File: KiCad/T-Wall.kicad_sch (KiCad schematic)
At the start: 52 parts, among them J1 IDC, J2 IDC, J3 IDC, J4 IDC, J5 IDC, J6 IDC, J7 IDC, J8 IDC, J9 2086-1107/300-000/997-607, U1 TCA9555PWR, U2 TCA9555PWR, U3 TCA9555PWR, U4 TCA9555PWR, U5 ESP32-S3-DevKitC, U6 SN74AHCT125RGYR, U9 TPS62A01APDDC

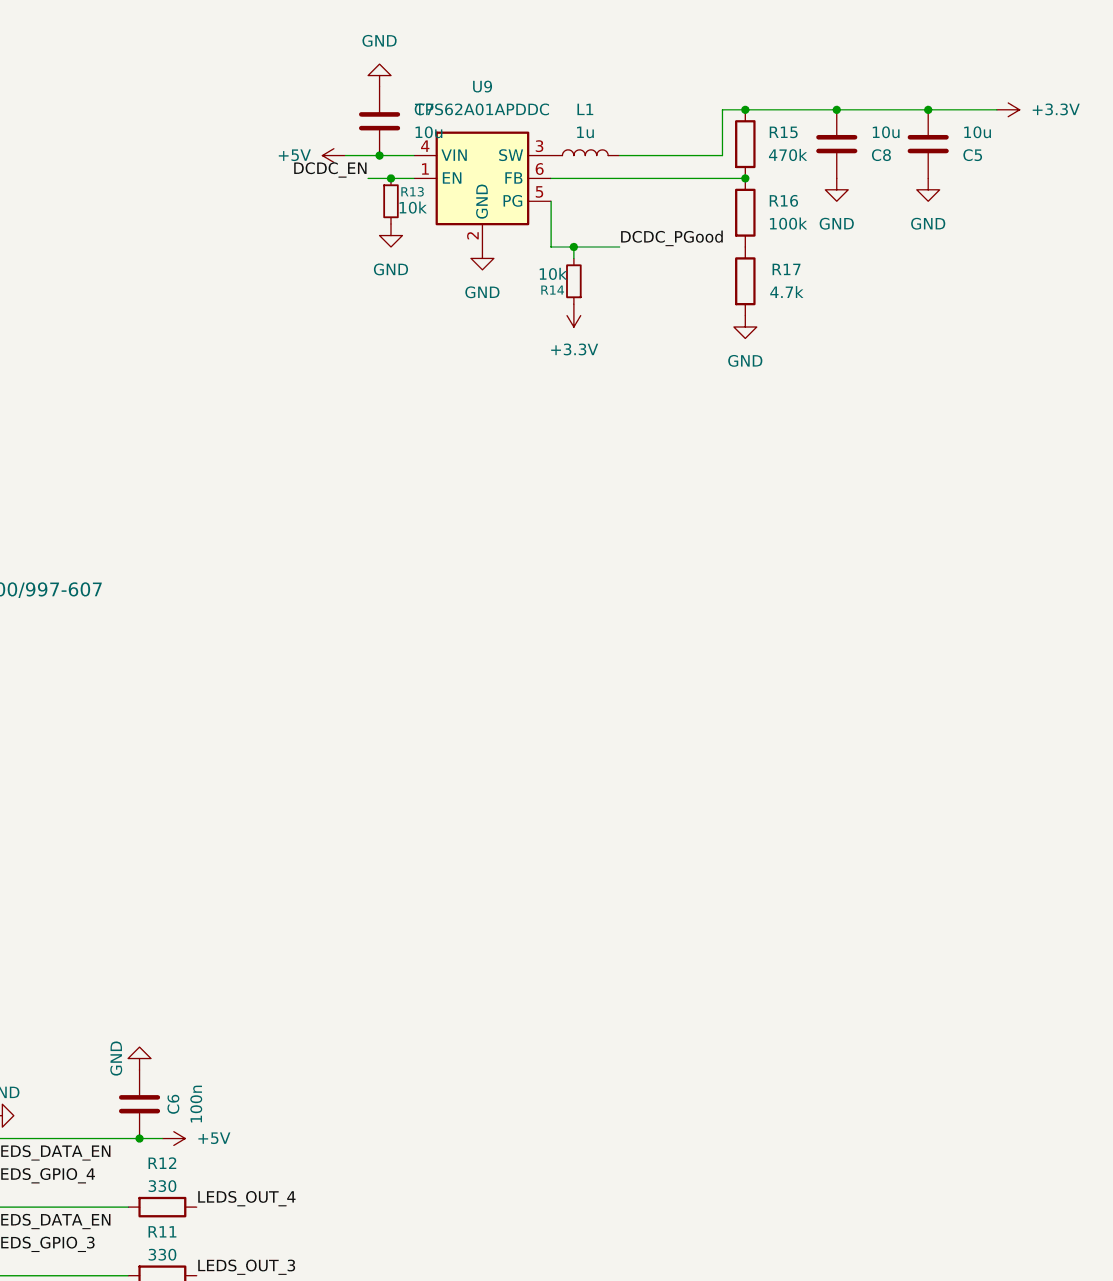
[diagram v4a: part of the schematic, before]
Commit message: PCB QOL: changed sizes to 0603 and moved vias away from pads
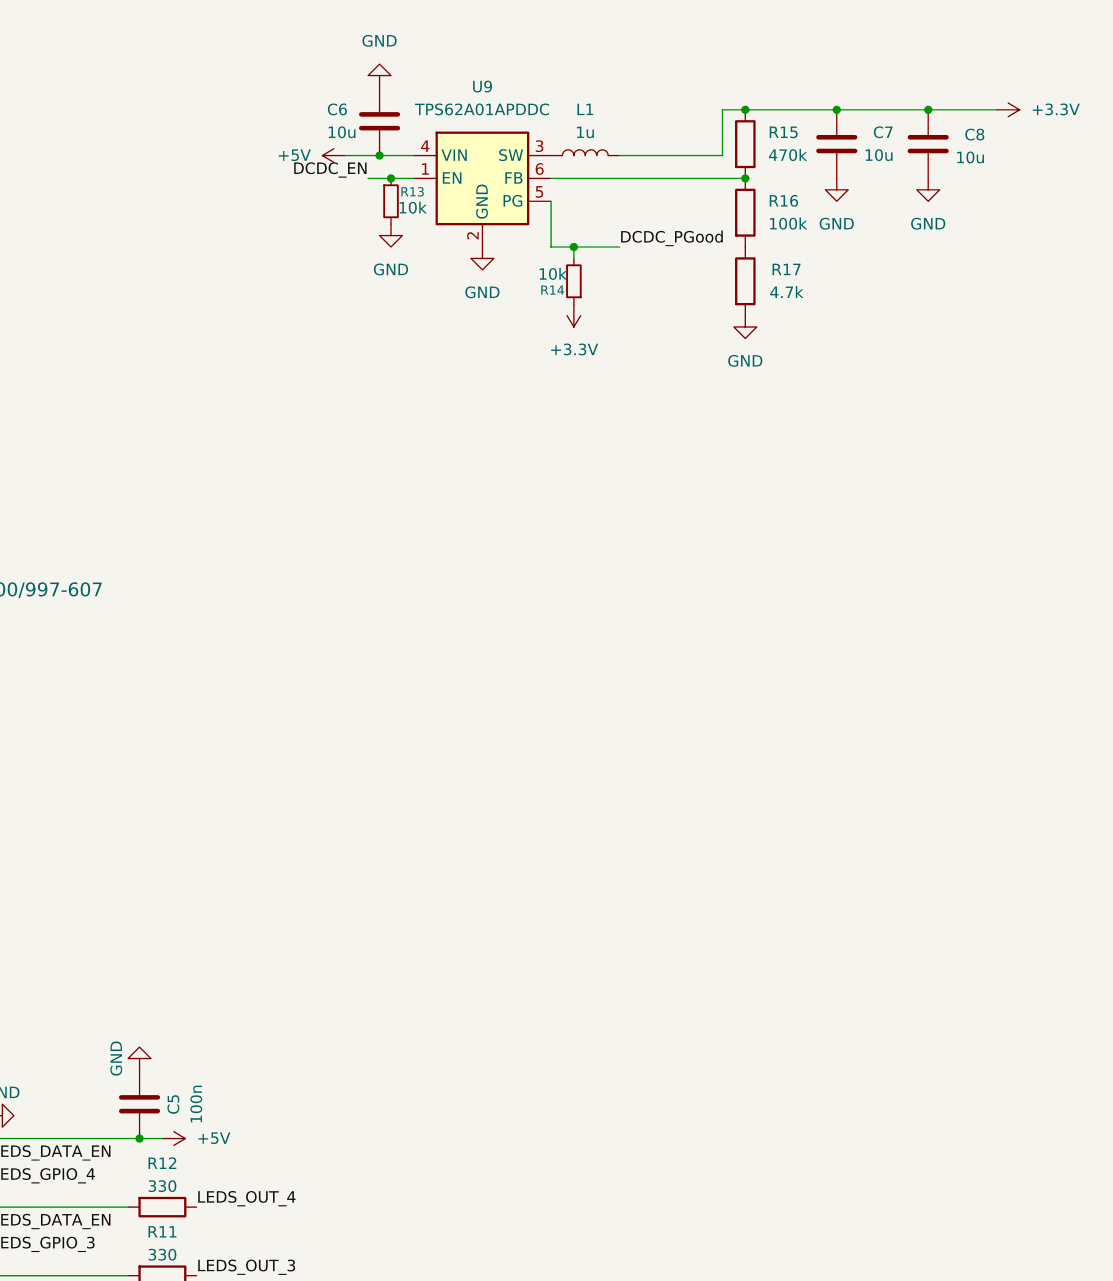
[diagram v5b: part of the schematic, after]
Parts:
- C1, C2, C3, C4: footprint Capacitor_SMD:C_0402_1005Metric_Pad0.74x0.62mm_HandSolder -> Capacitor_SMD:C_0603_1608Metric_Pad1.08x0.95mm_HandSolder; LCSC C1525 -> C14663
- C5: renamed from C6; footprint Capacitor_SMD:C_0402_1005Metric_Pad0.74x0.62mm_HandSolder -> Capacitor_SMD:C_0603_1608Metric_Pad1.08x0.95mm_HandSolder; LCSC C1525 -> C14663
- R1, R17, R2: footprint Resistor_SMD:R_0402_1005Metric_Pad0.72x0.64mm_HandSolder -> Resistor_SMD:R_0603_1608Metric_Pad0.98x0.95mm_HandSolder; LCSC C25900 -> C23162
- R10, R11, R12, R3: footprint Resistor_SMD:R_0402_1005Metric_Pad0.72x0.64mm_HandSolder -> Resistor_SMD:R_0603_1608Metric_Pad0.98x0.95mm_HandSolder; LCSC C25104 -> C23138
- R13, R14, R4, R5, R6, R7: footprint Resistor_SMD:R_0402_1005Metric_Pad0.72x0.64mm_HandSolder -> Resistor_SMD:R_0603_1608Metric_Pad0.98x0.95mm_HandSolder; LCSC C25744 -> C25804
- R15, R16: footprint Resistor_SMD:R_0201_0603Metric_Pad0.64x0.40mm_HandSolder -> Resistor_SMD:R_0603_1608Metric_Pad0.98x0.95mm_HandSolder
- renumbered C7 to C6, C8 to C7, C5 to C8
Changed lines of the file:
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@@
 			)
 		)
-		(property "Footprint" "Resistor_SMD:R_0402_1005Metric_Pad0.72x0.64mm_HandSolder"
+		(property "Footprint" "Resistor_SMD:R_0603_1608Metric_Pad0.98x0.95mm_HandSolder"
 			(at 224.79 155.702 90)
 			(effects
@@
 			)
 		)
-		(property "LCSC" "C25104"
+		(property "LCSC" "C23138"
 			(at 224.79 157.48 90)
 			(effects
@@
 		(on_board yes)
 		(dnp no)
-		(fields_autoplaced yes)
-		(property "Reference" "C7"
-			(at 350.52 33.0199 0)
+		(property "Reference" "C6"
+			(at 340.868 33.02 0)
 			(effects
 				(font
@@
 		)
 		(property "Value" "10u"
-			(at 350.52 35.5599 0)
+			(at 340.868 35.56 0)
 			(effects
 				(font
@@
 			(project "T-Wall"
 				(path "/7dc9e5b9-dd7a-4571-90c7-051ff63df3d4"
-					(reference "C7")
+					(reference "C6")
 					(unit 1)
 				)
@@
 			)
 		)
-		(property "Footprint" "Resistor_SMD:R_0402_1005Metric_Pad0.72x0.64mm_HandSolder"
+		(property "Footprint" "Resistor_SMD:R_0603_1608Metric_Pad0.98x0.95mm_HandSolder"
 			(at 224.79 148.082 90)
 			(effects
@@
 			)
 		)
-		(property "LCSC" "C25104"
+		(property "LCSC" "C23138"
 			(at 224.79 149.86 90)
 			(effects
@@
 			)
 		)
-		(property "Footprint" "Resistor_SMD:R_0402_1005Metric_Pad0.72x0.64mm_HandSolder"
+		(property "Footprint" "Resistor_SMD:R_0603_1608Metric_Pad0.98x0.95mm_HandSolder"
 			(at 181.61 83.058 90)
 			(effects
@@
 			)
 		)
-		(property "LCSC" "C25900"
+		(property "LCSC" "C23162"
 			(at 181.61 81.28 90)
 			(effects
@@
 			)
 		)
-		(property "Footprint" "Capacitor_SMD:C_0402_1005Metric_Pad0.74x0.62mm_HandSolder"
+		(property "Footprint" "Capacitor_SMD:C_0603_1608Metric_Pad1.08x0.95mm_HandSolder"
 			(at 86.36 345.1352 0)
 			(effects
@@
 			)
 		)
-		(property "LCSC" "C1525"
+		(property "LCSC" "C14663"
 			(at 90.17 344.17 90)
 			(effects
@@
 			)
 		)
-		(property "Footprint" "Resistor_SMD:R_0402_1005Metric_Pad0.72x0.64mm_HandSolder"
+		(property "Footprint" "Resistor_SMD:R_0603_1608Metric_Pad0.98x0.95mm_HandSolder"
 			(at 123.19 244.348 90)
 			(effects
@@
 			)
 		)
-		(property "LCSC" "C25744"
+		(property "LCSC" "C25804"
 			(at 123.19 242.57 90)
 			(effects
@@
 			)
 		)
-		(property "Footprint" "Resistor_SMD:R_0402_1005Metric_Pad0.72x0.64mm_HandSolder"
+		(property "Footprint" "Resistor_SMD:R_0603_1608Metric_Pad0.98x0.95mm_HandSolder"
 			(at 123.19 160.528 90)
 			(effects
@@
 			)
 		)
-		(property "LCSC" "C25744"
+		(property "LCSC" "C25804"
 			(at 123.19 158.75 90)
 			(effects
@@
 			)
 		)
-		(property "Footprint" "Capacitor_SMD:C_0402_1005Metric_Pad0.74x0.62mm_HandSolder"
+		(property "Footprint" "Capacitor_SMD:C_0603_1608Metric_Pad1.08x0.95mm_HandSolder"
 			(at 86.36 260.0452 0)
 			(effects
@@
 			)
 		)
-		(property "LCSC" "C1525"
+		(property "LCSC" "C14663"
 			(at 90.17 259.08 90)
 			(effects
@@
 		(on_board yes)
 		(dnp no)
-		(fields_autoplaced yes)
-		(property "Reference" "C5"
-			(at 411.48 38.1001 0)
+		(property "Reference" "C8"
+			(at 414.02 35.814 0)
 			(effects
 				(font
 					(size 1.27 1.27)
 				)
-				(justify left)
+				(justify right)
 			)
 		)
 		(property "Value" "10u"
-			(at 411.48 35.5601 0)
+			(at 414.02 38.354 0)
 			(effects
 				(font
 					(size 1.27 1.27)
 				)
-				(justify left)
+				(justify right)
 			)
 		)
@@
 			(project "T-Wall"
 				(path "/7dc9e5b9-dd7a-4571-90c7-051ff63df3d4"
-					(reference "C5")
+					(reference "C8")
 					(unit 1)
 				)
@@
 		(on_board yes)
 		(dnp no)
-		(fields_autoplaced yes)
-		(property "Reference" "C8"
-			(at 401.32 38.1001 0)
+		(property "Reference" "C7"
+			(at 403.86 35.56 0)
 			(effects
 				(font
 					(size 1.27 1.27)
 				)
-				(justify left)
+				(justify right)
 			)
 		)
 		(property "Value" "10u"
-			(at 401.32 35.5601 0)
+			(at 403.86 38.1 0)
 			(effects
 				(font
 					(size 1.27 1.27)
 				)
-				(justify left)
+				(justify right)
 			)
 		)
@@
 			(project "T-Wall"
 				(path "/7dc9e5b9-dd7a-4571-90c7-051ff63df3d4"
-					(reference "C8")
+					(reference "C7")
 					(unit 1)
 				)
@@
 			)
 		)
-		(property "Footprint" "Resistor_SMD:R_0201_0603Metric_Pad0.64x0.40mm_HandSolder"
+		(property "Footprint" "Resistor_SMD:R_0603_1608Metric_Pad0.98x0.95mm_HandSolder"
 			(at 385.572 44.45 90)
 			(effects
@@
 			)
 		)
-		(property "Footprint" "Resistor_SMD:R_0402_1005Metric_Pad0.72x0.64mm_HandSolder"
+		(property "Footprint" "Resistor_SMD:R_0603_1608Metric_Pad0.98x0.95mm_HandSolder"
 			(at 123.19 329.438 90)
 			(effects
@@
 			)
 		)
-		(property "LCSC" "C25744"
+		(property "LCSC" "C25804"
 			(at 123.19 327.66 90)
 			(effects
@@
 		(on_board yes)
 		(dnp no)
-		(property "Reference" "C6"
+		(property "Reference" "C5"
 			(at 323.85 143.51 90)
 			(effects
@@
 			)
 		)
-		(property "Footprint" "Capacitor_SMD:C_0402_1005Metric_Pad0.74x0.62mm_HandSolder"
+		(property "Footprint" "Capacitor_SMD:C_0603_1608Metric_Pad1.08x0.95mm_HandSolder"
 			(at 321.0052 147.32 0)
 			(effects
@@
 			)
 		)
-		(property "LCSC" "C1525"
+		(property "LCSC" "C14663"
 			(at 320.04 143.51 90)
 			(effects
@@
 			(project "T-Wall"
 				(path "/7dc9e5b9-dd7a-4571-90c7-051ff63df3d4"
-					(reference "C6")
+					(reference "C5")
 					(unit 1)
 				)
@@
 			)
 		)
-		(property "Footprint" "Resistor_SMD:R_0402_1005Metric_Pad0.72x0.64mm_HandSolder"
+		(property "Footprint" "Resistor_SMD:R_0603_1608Metric_Pad0.98x0.95mm_HandSolder"
 			(at 347.98 43.18 0)
 			(effects
@@
 			)
 		)
-		(property "LCSC" "C25744"
+		(property "LCSC" "C25804"
 			(at 347.98 43.18 0)
 			(effects
@@
 			)
 		)
-		(property "Footprint" "Resistor_SMD:R_0402_1005Metric_Pad0.72x0.64mm_HandSolder"
+		(property "Footprint" "Resistor_SMD:R_0603_1608Metric_Pad0.98x0.95mm_HandSolder"
 			(at 385.572 52.07 90)
 			(effects
@@
 			)
 		)
-		(property "LCSC" "C25900"
+		(property "LCSC" "C23162"
 			(at 387.35 52.07 90)
 			(effects
@@
 			)
 		)
-		(property "Footprint" "Resistor_SMD:R_0402_1005Metric_Pad0.72x0.64mm_HandSolder"
+		(property "Footprint" "Resistor_SMD:R_0603_1608Metric_Pad0.98x0.95mm_HandSolder"
 			(at 368.3 52.07 0)
 			(effects
@@
 			)
 		)
-		(property "LCSC" "C25744"
+		(property "LCSC" "C25804"
 			(at 368.3 52.07 0)
 			(effects
@@
 			)
 		)
-		(property "Footprint" "Resistor_SMD:R_0402_1005Metric_Pad0.72x0.64mm_HandSolder"
+		(property "Footprint" "Resistor_SMD:R_0603_1608Metric_Pad0.98x0.95mm_HandSolder"
 			(at 322.58 160.782 90)
 			(effects
@@
 			)
 		)
-		(property "LCSC" "C25104"
+		(property "LCSC" "C23138"
 			(at 322.58 162.56 90)
 			(effects
@@
 			)
 		)
-		(property "Footprint" "Resistor_SMD:R_0201_0603Metric_Pad0.64x0.40mm_HandSolder"
+		(property "Footprint" "Resistor_SMD:R_0603_1608Metric_Pad0.98x0.95mm_HandSolder"
 			(at 385.572 36.83 90)
 			(effects
@@
 			)
 		)
-		(property "Footprint" "Resistor_SMD:R_0402_1005Metric_Pad0.72x0.64mm_HandSolder"
+		(property "Footprint" "Resistor_SMD:R_0603_1608Metric_Pad0.98x0.95mm_HandSolder"
 			(at 181.61 82.042 90)
 			(effects
@@
 			)
 		)
-		(property "LCSC" "C25900"
+		(property "LCSC" "C23162"
 			(at 181.61 83.82 90)
 			(effects
@@
 			)
 		)
-		(property "Footprint" "Capacitor_SMD:C_0402_1005Metric_Pad0.74x0.62mm_HandSolder"
+		(property "Footprint" "Capacitor_SMD:C_0603_1608Metric_Pad1.08x0.95mm_HandSolder"
 			(at 86.36 89.8652 0)
 			(effects
@@
 			)
 		)
-		(property "LCSC" "C1525"
+		(property "LCSC" "C14663"
 			(at 90.17 88.9 90)
 			(effects
@@
 			)
 		)
-		(property "Footprint" "Capacitor_SMD:C_0402_1005Metric_Pad0.74x0.62mm_HandSolder"
+		(property "Footprint" "Capacitor_SMD:C_0603_1608Metric_Pad1.08x0.95mm_HandSolder"
 			(at 86.36 176.2252 0)
 			(effects
@@
 			)
 		)
-		(property "LCSC" "C1525"
+		(property "LCSC" "C14663"
 			(at 90.17 175.26 90)
 			(effects
@@
 			)
 		)
-		(property "Footprint" "Resistor_SMD:R_0402_1005Metric_Pad0.72x0.64mm_HandSolder"
+		(property "Footprint" "Resistor_SMD:R_0603_1608Metric_Pad0.98x0.95mm_HandSolder"
 			(at 322.58 153.162 90)
 			(effects
@@
 			)
 		)
-		(property "LCSC" "C25104"
+		(property "LCSC" "C23138"
 			(at 322.58 154.94 90)
 			(effects
@@
 			)
 		)
-		(property "Footprint" "Resistor_SMD:R_0402_1005Metric_Pad0.72x0.64mm_HandSolder"
+		(property "Footprint" "Resistor_SMD:R_0603_1608Metric_Pad0.98x0.95mm_HandSolder"
 			(at 123.19 74.168 90)
 			(effects
@@
 			)
 		)
-		(property "LCSC" "C25744"
+		(property "LCSC" "C25804"
 			(at 123.19 72.39 90)
 			(effects
